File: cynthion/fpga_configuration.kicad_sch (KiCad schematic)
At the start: 53 parts, among them IC1 ECP5-BGA256, J10 TC_SWD, J6 MCU_SWD, U6 ATSAMD11, U7 W25Q32JVSS

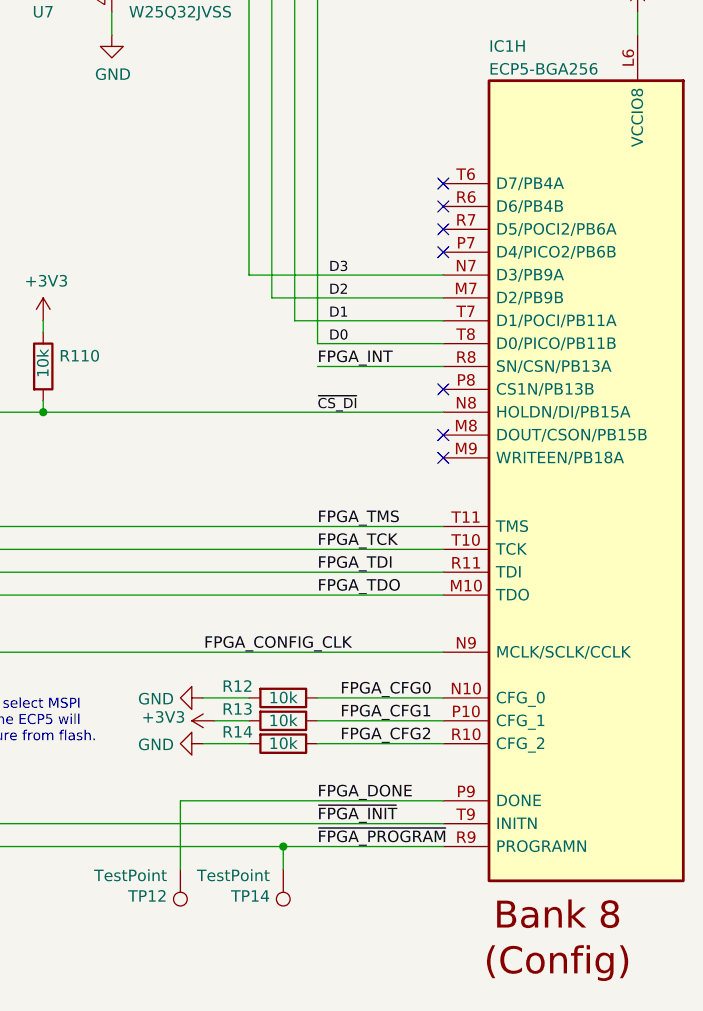
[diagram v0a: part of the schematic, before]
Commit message: hardware: change FPGA_INT pin assignment
This avoids an issue with FPGA_INT toggling during FPGA configuration.
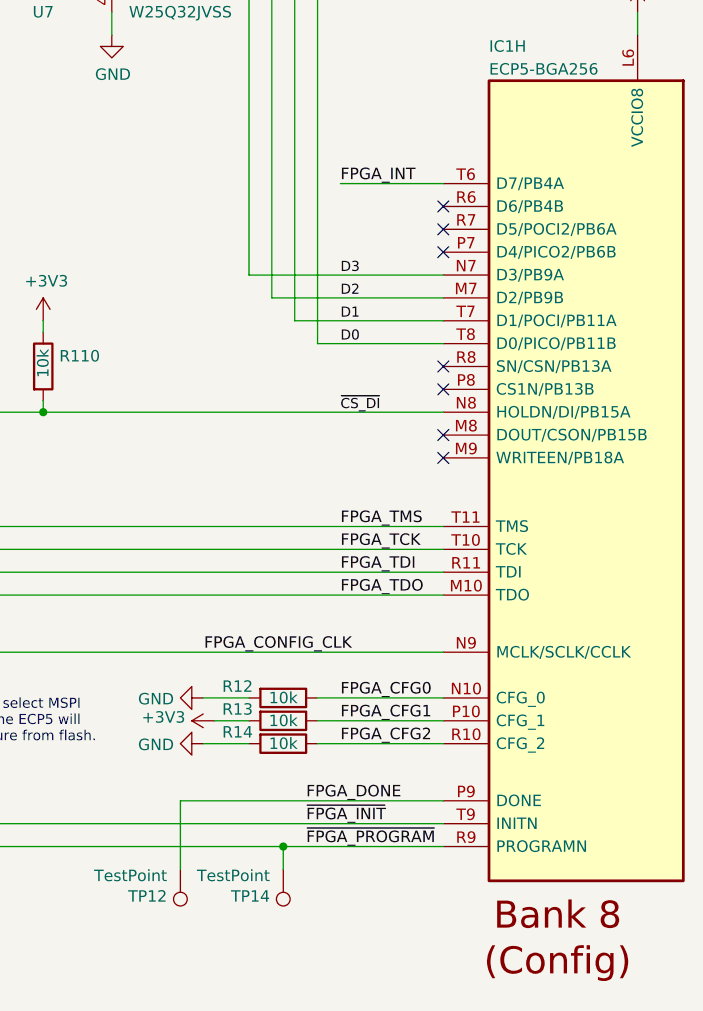
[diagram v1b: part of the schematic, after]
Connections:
- net FPGA_INT: now also IC1.T6 (D7/PB4A); no longer IC1.R8 (SN/CSN/PB13A)
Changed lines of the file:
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@@
   )
   (no_connect (at 247.65 90.17))
-  (no_connect (at 247.65 67.31))
+  (no_connect (at 247.65 87.63))
   (no_connect (at 247.65 74.93))
   (no_connect (at 247.65 95.25))
@@
     (stroke (width 0) (type default) (color 0 0 0 0))
   )
-  (wire (pts (xy 247.65 87.63) (xy 233.68 87.63))
+  (wire (pts (xy 247.65 67.31) (xy 236.22 67.31))
     (stroke (width 0) (type default) (color 0 0 0 0))
   )
@@
     (effects (font (size 1.27 1.27)) (justify left bottom))
   )
-  (label "FPGA_TMS" (at 233.68 105.41 0)
-    (effects (font (size 1.27 1.27)) (justify left bottom))
-  )
-  (label "D1" (at 234.95 82.55 0)
+  (label "FPGA_TMS" (at 236.22 105.41 0)
+    (effects (font (size 1.27 1.27)) (justify left bottom))
+  )
+  (label "D1" (at 236.22 82.55 0)
     (effects (font (size 1.1176 1.1176)) (justify left bottom))
   )
-  (label "~{FPGA_INIT}" (at 233.68 138.43 0)
+  (label "~{FPGA_INIT}" (at 232.41 138.43 0)
     (effects (font (size 1.27 1.27)) (justify left bottom))
   )
@@
     (effects (font (size 1.27 1.27)) (justify left bottom))
   )
-  (label "D0" (at 234.95 85.09 0)
+  (label "D0" (at 236.22 85.09 0)
     (effects (font (size 1.1176 1.1176)) (justify left bottom))
   )
-  (label "D3" (at 234.95 77.47 0)
+  (label "D3" (at 236.22 77.47 0)
     (effects (font (size 1.1176 1.1176)) (justify left bottom))
   )
@@
     (effects (font (size 1.27 1.27)) (justify left bottom))
   )
-  (label "FPGA_INT" (at 233.68 87.63 0)
-    (effects (font (size 1.27 1.27)) (justify left bottom))
-  )
-  (label "D2" (at 234.95 80.01 0)
+  (label "FPGA_INT" (at 236.22 67.31 0)
+    (effects (font (size 1.27 1.27)) (justify left bottom))
+  )
+  (label "D2" (at 236.22 80.01 0)
     (effects (font (size 1.1176 1.1176)) (justify left bottom))
   )
-  (label "FPGA_DONE" (at 233.68 135.89 0)
-    (effects (font (size 1.27 1.27)) (justify left bottom))
-  )
-  (label "FPGA_TDO" (at 233.68 113.03 0)
+  (label "FPGA_DONE" (at 232.41 135.89 0)
+    (effects (font (size 1.27 1.27)) (justify left bottom))
+  )
+  (label "FPGA_TDO" (at 236.22 113.03 0)
     (effects (font (size 1.27 1.27)) (justify left bottom))
   )
@@
     (effects (font (size 1.27 1.27)) (justify left bottom))
   )
-  (label "~{FPGA_PROGRAM}" (at 233.68 140.97 0)
+  (label "~{FPGA_PROGRAM}" (at 232.41 140.97 0)
     (effects (font (size 1.27 1.27)) (justify left bottom))
   )
@@
     (effects (font (size 1.27 1.27)) (justify left bottom))
   )
-  (label "FPGA_TDI" (at 233.68 110.49 0)
+  (label "FPGA_TDI" (at 236.22 110.49 0)
     (effects (font (size 1.27 1.27)) (justify left bottom))
   )
@@
     (effects (font (size 1.27 1.27)) (justify right bottom))
   )
-  (label "FPGA_TCK" (at 233.68 107.95 0)
+  (label "FPGA_TCK" (at 236.22 107.95 0)
     (effects (font (size 1.27 1.27)) (justify left bottom))
   )
@@
     (effects (font (size 1.27 1.27)) (justify left bottom))
   )
-  (label "~{CS_DI}" (at 233.68 92.71 0)
+  (label "~{CS_DI}" (at 236.22 92.71 0)
     (effects (font (size 1.1176 1.1176)) (justify left bottom))
   )

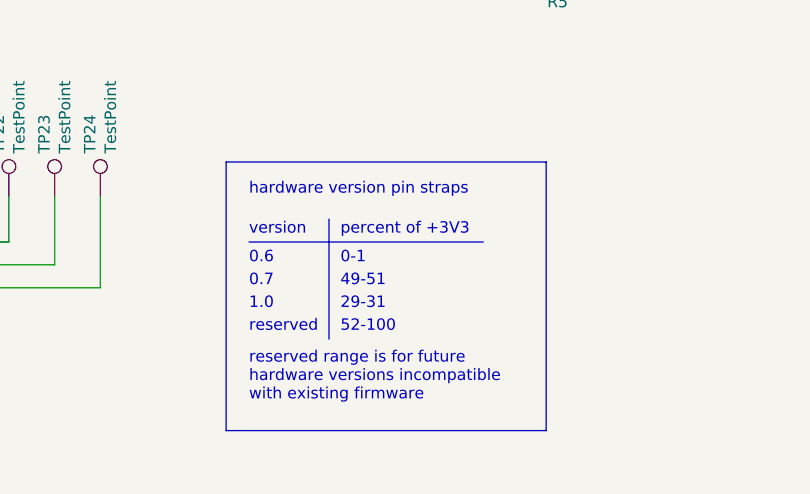
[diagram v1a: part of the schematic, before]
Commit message: correct hardware version pin strap table
fix #7
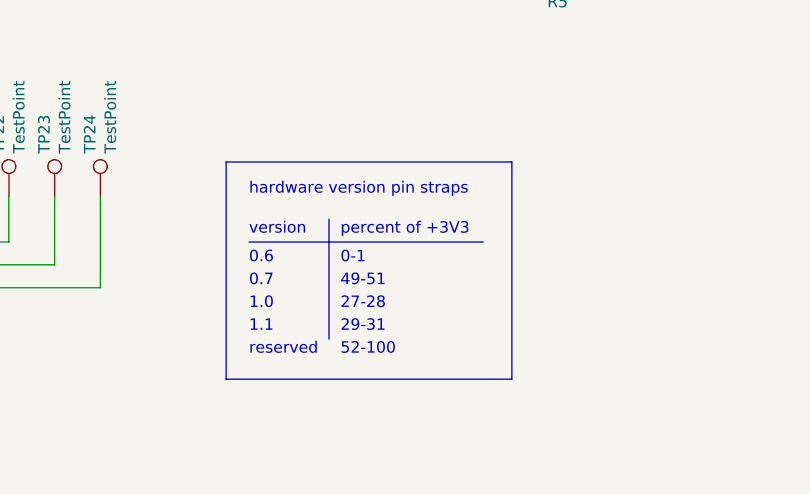
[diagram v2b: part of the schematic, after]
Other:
- note added: "1.1"
- note added: "27-28"
- note removed: "reserved range is for future hardware versions incompatible with existing firmware"
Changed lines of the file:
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@@
     (stroke (width 0) (type default) (color 0 0 0 0))
   )
-  (polyline (pts (xy 133.35 161.29) (xy 168.91 161.29))
+  (polyline (pts (xy 133.35 161.29) (xy 165.1 161.29))
     (stroke (width 0) (type default) (color 0 0 0 0))
   )
@@
     (stroke (width 0) (type default) (color 0 0 0 0))
   )
-  (polyline (pts (xy 133.35 161.29) (xy 133.35 191.135))
+  (polyline (pts (xy 133.35 161.29) (xy 133.35 185.42))
     (stroke (width 0) (type default) (color 0 0 0 0))
   )
@@
     (stroke (width 0) (type default) (color 0 0 0 0))
   )
-  (polyline (pts (xy 168.91 161.29) (xy 168.91 191.135))
+  (polyline (pts (xy 165.1 161.29) (xy 165.1 185.42))
     (stroke (width 0) (type default) (color 0 0 0 0))
   )
@@
     (stroke (width 0) (type default) (color 0 0 0 0))
   )
-  (polyline (pts (xy 168.91 191.135) (xy 133.35 191.135))
+  (polyline (pts (xy 165.1 185.42) (xy 133.35 185.42))
     (stroke (width 0) (type default) (color 0 0 0 0))
   )
@@
     (effects (font (size 3.5052 3.5052)) (justify left bottom))
   )
-  (text "reserved" (at 135.89 180.34 0)
+  (text "reserved" (at 135.89 182.88 0)
+    (effects (font (size 1.27 1.27)) (justify left bottom))
+  )
+  (text "27-28" (at 146.05 177.8 0)
     (effects (font (size 1.27 1.27)) (justify left bottom))
   )
@@
     (effects (font (size 1.1176 1.1176)) (justify left bottom))
   )
-  (text "52-100" (at 146.05 180.34 0)
+  (text "52-100" (at 146.05 182.88 0)
     (effects (font (size 1.27 1.27)) (justify left bottom))
   )
@@
   )
   (text "percent of +3V3" (at 146.05 169.545 0)
-    (effects (font (size 1.27 1.27)) (justify left bottom))
-  )
-  (text "1.0" (at 135.89 177.8 0)
     (effects (font (size 1.27 1.27)) (justify left bottom))
   )
@@
     (effects (font (size 1.27 1.27)) (justify left bottom))
   )
+  (text "29-31" (at 146.05 180.34 0)
+    (effects (font (size 1.27 1.27)) (justify left bottom))
+  )
   (text "0.6" (at 135.89 172.72 0)
     (effects (font (size 1.27 1.27)) (justify left bottom))
@@
     (effects (font (size 1.27 1.27)) (justify left bottom))
   )
-  (text "29-31" (at 146.05 177.8 0)
+  (text "1.0" (at 135.89 177.8 0)
     (effects (font (size 1.27 1.27)) (justify left bottom))
   )
@@
     (effects (font (size 1.1176 1.1176)) (justify left bottom))
   )
-  (text "reserved range is for future\nhardware versions incompatible\nwith existing firmware"
-    (at 135.89 187.96 0)
-    (effects (font (size 1.27 1.27)) (justify left bottom))
-  )
+  (text "1.1" (at 135.89 180.34 0)
+    (effects (font (size 1.27 1.27)) (justify left bottom))
+  )
